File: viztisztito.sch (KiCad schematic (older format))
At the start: 18 parts

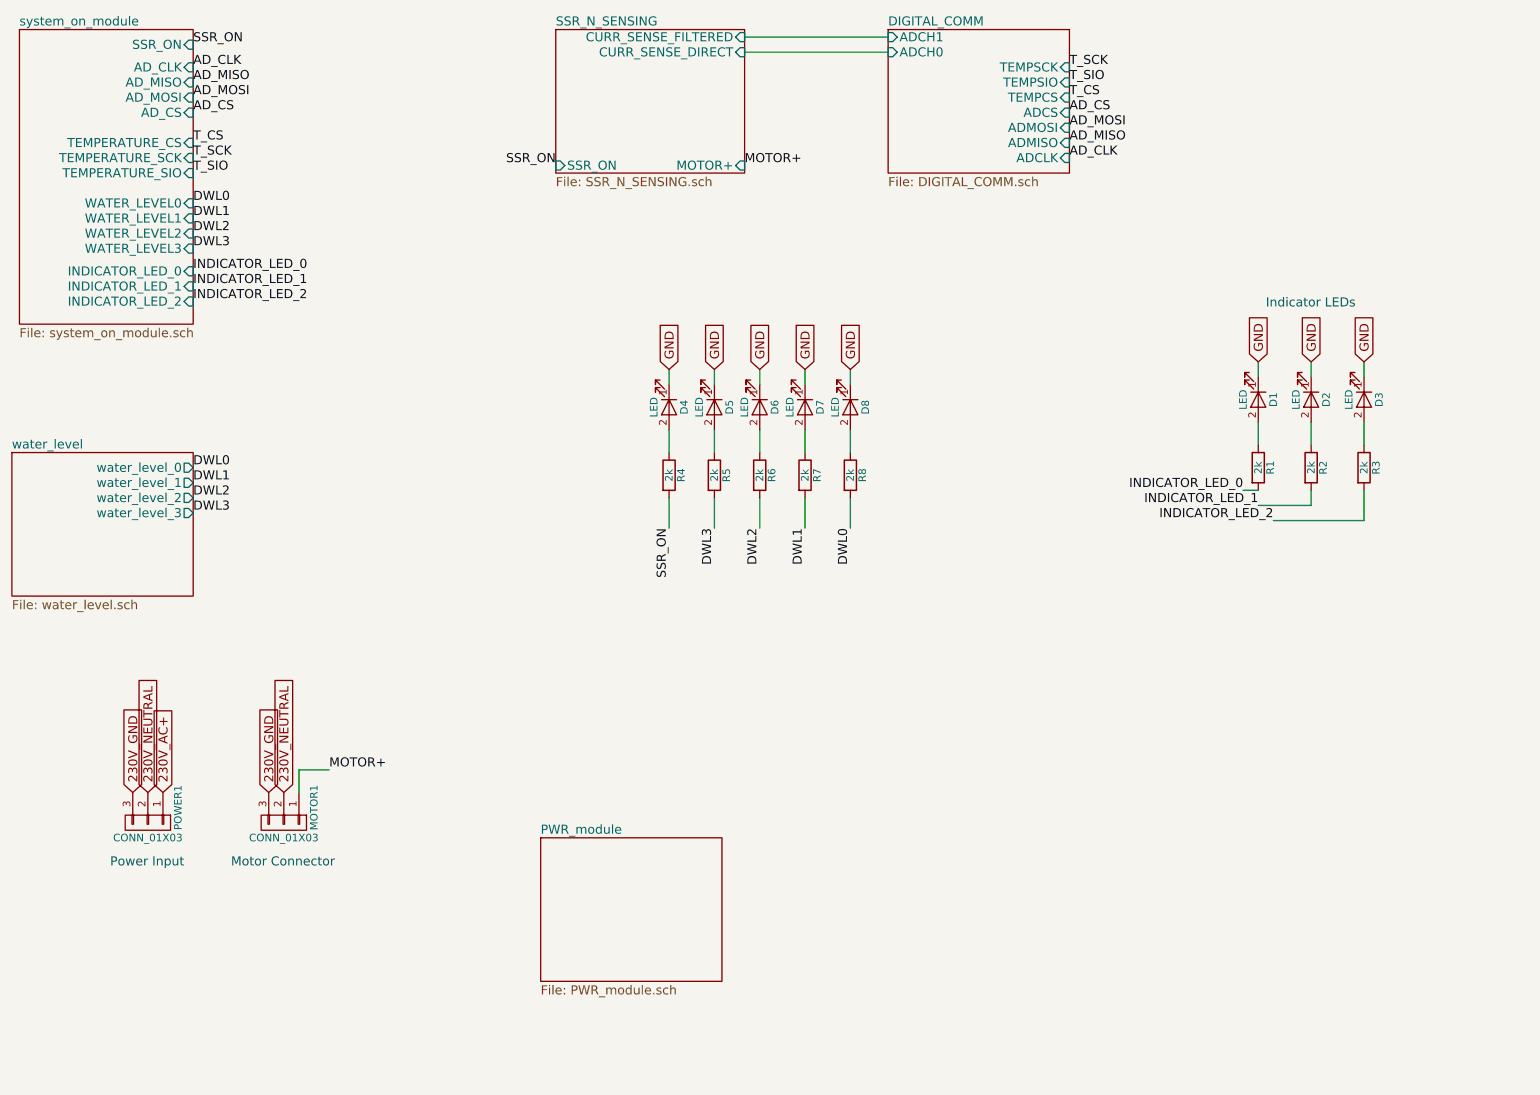
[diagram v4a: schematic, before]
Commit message: this version contains the datasheets and the footprints of the parts
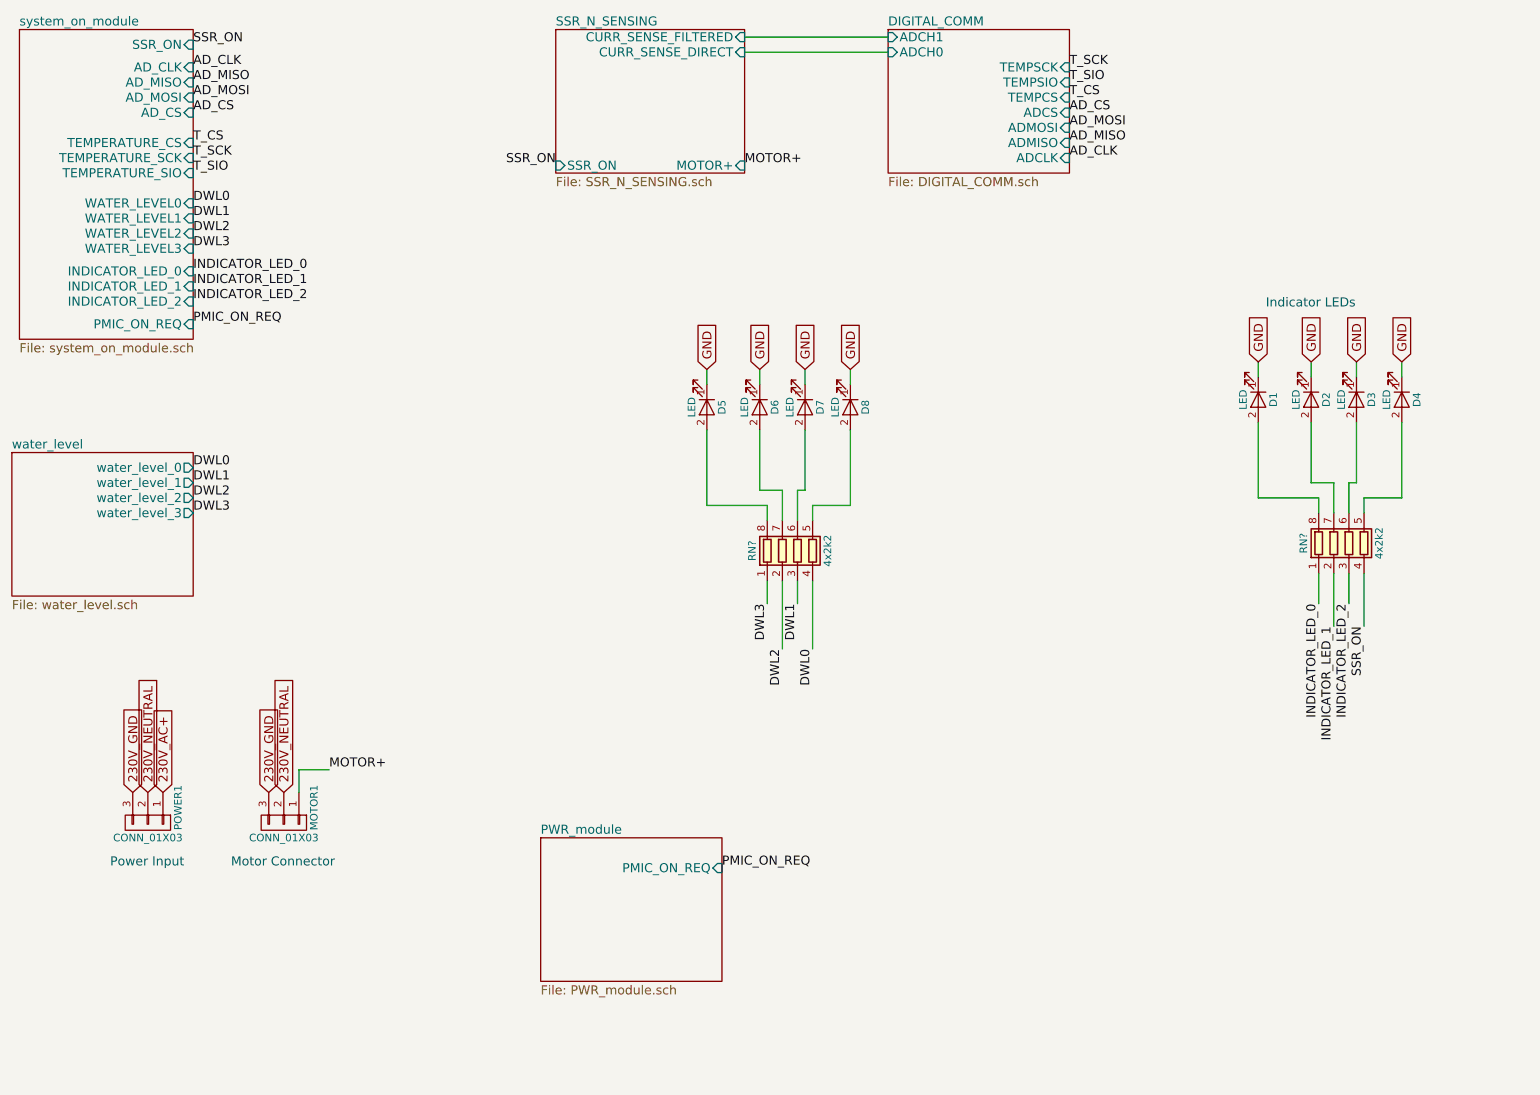
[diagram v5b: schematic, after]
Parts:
- removed R1, R2, R3, R4, R5, R6, R7, R8: 2k, Resistors_SMD:R_1206_HandSoldering, symbol R
- added RN? (x2): 4x2k2, symbol R_Pack04
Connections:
- net DWL0: now also RN?.4 (R4.1)
- net DWL1: now also RN?.3 (R3.1)
- net DWL2: now also RN?.2 (R2.1)
- net DWL3: now also RN?.1 (R1.1)
- net INDICATOR_LED_0: now also RN?.1 (R1.1)
- net INDICATOR_LED_1: now also RN?.2 (R2.1)
- net INDICATOR_LED_2: now also RN?.3 (R3.1)
- net SSR_ON: now also RN?.4 (R4.1)
- net at D2.2 (A): now also RN?.7 (R2.2)
- net at D1.2 (A): now also RN?.8 (R1.2)
- net at D3.2 (A): now also RN?.6 (R3.2)
- net at D4.2 (A): now also RN?.5 (R4.2)
- net at D5.2 (A): now also RN?.8 (R1.2)
- net at D6.2 (A): now also RN?.7 (R2.2)
- net at D7.2 (A): now also RN?.6 (R3.2)
- net at D8.2 (A): now also RN?.5 (R4.2)
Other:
- moved on the sheet: D3, D4, D5
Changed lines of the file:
@@
 F0 "PWR_module" 60
 F1 "PWR_module.sch" 60
+F2 "PMIC_ON_REQ" I R 5950 6550 60
 $EndSheet
 $Sheet
@@
 230V_GND
 $Comp
-L R R2
-U 1 1 593FD7AC
-P 9850 3900
-F 0 "R2" V 9930 3900 50  0000 C CNN
-F 1 "2k" V 9850 3900 50  0000 C CNN
-F 2 "Resistors_SMD:R_1206_HandSoldering" V 9780 3900 50  0001 C CNN
-F 3 "http://hu.farnell.com/multicomp/mcwr12x3300ftl/res-thick-film-330r-1-0-25w-1206/dp/2447504" H 9850 3900 50  0001 C CNN
-	1    9850 3900
-	1    0    0    -1
-$EndComp
-$Comp
 L LED D2
 U 1 1 593FD84F
@@
 	9850 3200 9850 3300
 Wire Wire Line
-	9850 3600 9850 3750
-$Comp
-L R R1
-U 1 1 593FEF66
-P 9500 3900
-F 0 "R1" V 9580 3900 50  0000 C CNN
-F 1 "2k" V 9500 3900 50  0000 C CNN
-F 2 "Resistors_SMD:R_1206_HandSoldering" V 9430 3900 50  0001 C CNN
-F 3 "http://hu.farnell.com/multicomp/mcwr12x3300ftl/res-thick-film-330r-1-0-25w-1206/dp/2447504" H 9500 3900 50  0001 C CNN
-	1    9500 3900
-	1    0    0    -1
-$EndComp
+	9850 3600 9850 4000
 $Comp
 L LED D1
@@
 	9500 3200 9500 3300
 Wire Wire Line
-	9500 3600 9500 3750
-$Comp
-L R R3
-U 1 1 593FF0D5
-P 10200 3900
-F 0 "R3" V 10280 3900 50  0000 C CNN
-F 1 "2k" V 10200 3900 50  0000 C CNN
-F 2 "Resistors_SMD:R_1206_HandSoldering" V 10130 3900 50  0001 C CNN
-F 3 "http://hu.farnell.com/multicomp/mcwr12x3300ftl/res-thick-film-330r-1-0-25w-1206/dp/2447504" H 10200 3900 50  0001 C CNN
-	1    10200 3900
-	1    0    0    -1
-$EndComp
+	9500 3600 9500 4100
 $Comp
 L LED D3
 U 1 1 593FF0DB
-P 10200 3450
-F 0 "D3" H 10200 3550 50  0000 C CNN
-F 1 "LED" H 10200 3350 50  0000 C CNN
-F 2 "LEDs:LED_1206" H 10200 3450 50  0001 C CNN
-F 3 "http://hu.farnell.com/lumex/sml-lx15syc-tr/led-yellow-3mm-60mcd-590nm/dp/2062220" H 10200 3450 50  0001 C CNN
-	1    10200 3450
-	0    1    1    0
-$EndComp
-Text GLabel 10200 3200 1    60   Input ~ 0
-GND
-Wire Wire Line
-	10200 3200 10200 3300
-Wire Wire Line
-	10200 3600 10200 3750
-Wire Wire Line
-	9400 4050 9500 4050
-Wire Wire Line
-	9500 4150 9850 4150
-Wire Wire Line
-	9850 4150 9850 4050
-Wire Wire Line
-	9600 4250 10200 4250
-Wire Wire Line
-	10200 4250 10200 4050
+P 10150 3450
+F 0 "D3" H 10150 3550 50  0000 C CNN
+F 1 "LED" H 10150 3350 50  0000 C CNN
+F 2 "LEDs:LED_1206" H 10150 3450 50  0001 C CNN
+F 3 "http://hu.farnell.com/lumex/sml-lx15syc-tr/led-yellow-3mm-60mcd-590nm/dp/2062220" H 10150 3450 50  0001 C CNN
+	1    10150 3450
+	0    1    1    0
+$EndComp
+Text GLabel 10150 3200 1    60   Input ~ 0
+GND
+Wire Wire Line
+	10150 3200 10150 3300
+Wire Wire Line
+	10150 3600 10150 4000
 Text Notes 9550 2850 0    60   ~ 0
 Indicator LEDs
 $Comp
-L R R4
-U 1 1 59406395
-P 5600 3950
-F 0 "R4" V 5680 3950 50  0000 C CNN
-F 1 "2k" V 5600 3950 50  0000 C CNN
-F 2 "Resistors_SMD:R_1206_HandSoldering" V 5530 3950 50  0001 C CNN
-F 3 "http://hu.farnell.com/multicomp/mcwr12x1001ftl/res-thick-film-1k-1-0-25w-1206/dp/2447473" H 5600 3950 50  0001 C CNN
-	1    5600 3950
-	1    0    0    -1
-$EndComp
-$Comp
 L LED D4
 U 1 1 5940639C
-P 5600 3500
-F 0 "D4" H 5600 3600 50  0000 C CNN
-F 1 "LED" H 5600 3400 50  0000 C CNN
-F 2 "LEDs:LED_1206" H 5600 3500 50  0001 C CNN
-F 3 "http://hu.farnell.com/lumex/sml-lx15syc-tr/led-yellow-3mm-60mcd-590nm/dp/2062220" H 5600 3500 50  0001 C CNN
-	1    5600 3500
-	0    1    1    0
-$EndComp
-Text GLabel 5600 3250 1    60   Input ~ 0
-GND
-Wire Wire Line
-	5600 3250 5600 3350
-Wire Wire Line
-	5600 3650 5600 3800
-Wire Wire Line
-	5600 4300 5600 4100
-Text Label 5600 4300 3    60   ~ 0
+P 10450 3450
+F 0 "D4" H 10450 3550 50  0000 C CNN
+F 1 "LED" H 10450 3350 50  0000 C CNN
+F 2 "LEDs:LED_1206" H 10450 3450 50  0001 C CNN
+F 3 "http://hu.farnell.com/lumex/sml-lx15syc-tr/led-yellow-3mm-60mcd-590nm/dp/2062220" H 10450 3450 50  0001 C CNN
+	1    10450 3450
+	0    1    1    0
+$EndComp
+Text GLabel 10450 3200 1    60   Input ~ 0
+GND
+Wire Wire Line
+	10450 3200 10450 3300
+Wire Wire Line
+	10450 3600 10450 4100
+Text Label 10200 4950 3    60   ~ 0
 SSR_ON
-$Comp
-L R R5
-U 1 1 59406BBF
-P 5900 3950
-F 0 "R5" V 5980 3950 50  0000 C CNN
-F 1 "2k" V 5900 3950 50  0000 C CNN
-F 2 "Resistors_SMD:R_1206_HandSoldering" V 5830 3950 50  0001 C CNN
-F 3 "http://hu.farnell.com/multicomp/mcwr12x1001ftl/res-thick-film-1k-1-0-25w-1206/dp/2447473" H 5900 3950 50  0001 C CNN
-	1    5900 3950
-	1    0    0    -1
-$EndComp
 $Comp
 L LED D5
 U 1 1 59406BC6
-P 5900 3500
-F 0 "D5" H 5900 3600 50  0000 C CNN
-F 1 "LED" H 5900 3400 50  0000 C CNN
-F 2 "LEDs:LED_1206" H 5900 3500 50  0001 C CNN
-F 3 "http://hu.farnell.com/lumex/sml-lx15syc-tr/led-yellow-3mm-60mcd-590nm/dp/2062220" H 5900 3500 50  0001 C CNN
-	1    5900 3500
-	0    1    1    0
-$EndComp
-Text GLabel 5900 3250 1    60   Input ~ 0
-GND
-Wire Wire Line
-	5900 3250 5900 3350
-Wire Wire Line
-	5900 3650 5900 3800
-Wire Wire Line
-	5900 4300 5900 4100
-$Comp
-L R R6
-U 1 1 59406CAD
-P 6200 3950
-F 0 "R6" V 6280 3950 50  0000 C CNN
-F 1 "2k" V 6200 3950 50  0000 C CNN
-F 2 "Resistors_SMD:R_1206_HandSoldering" V 6130 3950 50  0001 C CNN
-F 3 "http://hu.farnell.com/multicomp/mcwr12x1001ftl/res-thick-film-1k-1-0-25w-1206/dp/2447473" H 6200 3950 50  0001 C CNN
-	1    6200 3950
-	1    0    0    -1
-$EndComp
+P 5850 3500
+F 0 "D5" H 5850 3600 50  0000 C CNN
+F 1 "LED" H 5850 3400 50  0000 C CNN
+F 2 "LEDs:LED_1206" H 5850 3500 50  0001 C CNN
+F 3 "http://hu.farnell.com/lumex/sml-lx15syc-tr/led-yellow-3mm-60mcd-590nm/dp/2062220" H 5850 3500 50  0001 C CNN
+	1    5850 3500
+	0    1    1    0
+$EndComp
+Text GLabel 5850 3250 1    60   Input ~ 0
+GND
+Wire Wire Line
+	5850 3250 5850 3350
 $Comp
 L LED D6
@@
 Wire Wire Line
 	6200 3250 6200 3350
-Wire Wire Line
-	6200 3650 6200 3800
-Wire Wire Line
-	6200 4300 6200 4100
-$Comp
-L R R7
-U 1 1 59406D8D
-P 6500 3950
-F 0 "R7" V 6580 3950 50  0000 C CNN
-F 1 "2k" V 6500 3950 50  0000 C CNN
-F 2 "Resistors_SMD:R_1206_HandSoldering" V 6430 3950 50  0001 C CNN
-F 3 "http://hu.farnell.com/multicomp/mcwr12x1001ftl/res-thick-film-1k-1-0-25w-1206/dp/2447473" H 6500 3950 50  0001 C CNN
-	1    6500 3950
-	1    0    0    -1
-$EndComp
 $Comp
 L LED D7
@@
 Wire Wire Line
 	6500 3250 6500 3350
-Wire Wire Line
-	6500 3650 6500 3800
-Wire Wire Line
-	6500 4300 6500 4100
-$Comp
-L R R8
-U 1 1 59406E7B
-P 6800 3950
-F 0 "R8" V 6880 3950 50  0000 C CNN
-F 1 "2k" V 6800 3950 50  0000 C CNN
-F 2 "Resistors_SMD:R_1206_HandSoldering" V 6730 3950 50  0001 C CNN
-F 3 "http://hu.farnell.com/multicomp/mcwr12x1001ftl/res-thick-film-1k-1-0-25w-1206/dp/2447473" H 6800 3950 50  0001 C CNN
-	1    6800 3950
-	1    0    0    -1
-$EndComp
 $Comp
 L LED D8
@@
 Wire Wire Line
 	6800 3250 6800 3350
-Wire Wire Line
-	6800 3650 6800 3800
-Wire Wire Line
-	6800 4300 6800 4100
-Text Label 5900 4300 3    60   ~ 0
+Text Label 6250 4800 3    60   ~ 0
 DWL3
-Text Label 6200 4300 3    60   ~ 0
+Text Label 6350 5100 3    60   ~ 0
 DWL2
-Text Label 6500 4300 3    60   ~ 0
+Text Label 6450 4800 3    60   ~ 0
 DWL1
-Text Label 6800 4300 3    60   ~ 0
+Text Label 6550 5100 3    60   ~ 0
 DWL0
 $Sheet
-S 1300 1000 1150 1950
+S 1300 1000 1150 2050
 U 599A5341
 F0 "system_on_module" 60
@@
 F15 "INDICATOR_LED_1" I R 2450 2700 60
 F16 "INDICATOR_LED_2" I R 2450 2800 60
+F17 "PMIC_ON_REQ" I R 2450 2950 60
 $EndSheet
 Text Label 6100 1900 0    60   ~ 0
@@
 Text Label 2450 2800 0    60   ~ 0
 INDICATOR_LED_2
-Text Label 9400 4050 2    60   ~ 0
+Text Label 9900 4800 3    60   ~ 0
 INDICATOR_LED_0
-Text Label 9500 4150 2    60   ~ 0
+Text Label 10000 4950 3    60   ~ 0
 INDICATOR_LED_1
-Text Label 9600 4250 2    60   ~ 0
+Text Label 10100 4800 3    60   ~ 0
 INDICATOR_LED_2
+Text Label 2450 2950 0    60   ~ 0
+PMIC_ON_REQ
+Text Label 5950 6550 0    60   ~ 0
+PMIC_ON_REQ
+$Comp
+L R_Pack04 RN?
+U 1 1 59A7A20E
+P 6450 4450
+F 0 "RN?" V 6150 4450 50  0000 C CNN
+F 1 "4x2k2" V 6650 4450 50  0000 C CNN
+F 2 "" V 6725 4450 50  0001 C CNN
+F 3 "http://hu.farnell.com/yageo-phycomp/yc164-jr-072k2l/resistor-array-arv241-1206-2k2/dp/9234535" H 6450 4450 50  0001 C CNN
+	1    6450 4450
+	1    0    0    -1
+$EndComp
+$Comp
+L R_Pack04 RN?
+U 1 1 59A7A83E
+P 10100 4400
+F 0 "RN?" V 9800 4400 50  0000 C CNN
+F 1 "4x2k2" V 10300 4400 50  0000 C CNN
+F 2 "" V 10375 4400 50  0001 C CNN
+F 3 "http://hu.farnell.com/yageo-phycomp/yc164-jr-072k2l/resistor-array-arv241-1206-2k2/dp/9234535" H 10100 4400 50  0001 C CNN
+	1    10100 4400
+	1    0    0    -1
+$EndComp
+Wire Wire Line
+	10200 4950 10200 4600
+Wire Wire Line
+	10100 4800 10100 4600
+Wire Wire Line
+	10000 4950 10000 4600
+Wire Wire Line
+	9900 4800 9900 4600
+Wire Wire Line
+	10150 4000 10100 4000
+Wire Wire Line
+	10100 4000 10100 4200
+Wire Wire Line
+	9850 4000 10000 4000
+Wire Wire Line
+	10000 4000 10000 4200
+Wire Wire Line
+	9500 4100 9900 4100
+Wire Wire Line
+	9900 4100 9900 4200
+Wire Wire Line
+	10450 4100 10200 4100
+Wire Wire Line
+	10200 4100 10200 4200
+Wire Wire Line
+	6550 5100 6550 4650
+Wire Wire Line
+	6450 4800 6450 4650
+Wire Wire Line
+	6350 5100 6350 4650
+Wire Wire Line
+	6250 4800 6250 4650
+Wire Wire Line
+	6200 3650 6200 4050
+Wire Wire Line
+	5850 3650 5850 4150
+Wire Wire Line
+	6500 3650 6500 4050
+Wire Wire Line
+	6800 3650 6800 4150
+Wire Wire Line
+	6500 4050 6450 4050
+Wire Wire Line
+	6450 4050 6450 4250
+Wire Wire Line
+	6200 4050 6350 4050
+Wire Wire Line
+	6350 4050 6350 4250
+Wire Wire Line
+	5850 4150 6250 4150
+Wire Wire Line
+	6250 4150 6250 4250
+Wire Wire Line
+	6800 4150 6550 4150
+Wire Wire Line
+	6550 4150 6550 4250
 $EndSCHEMATC

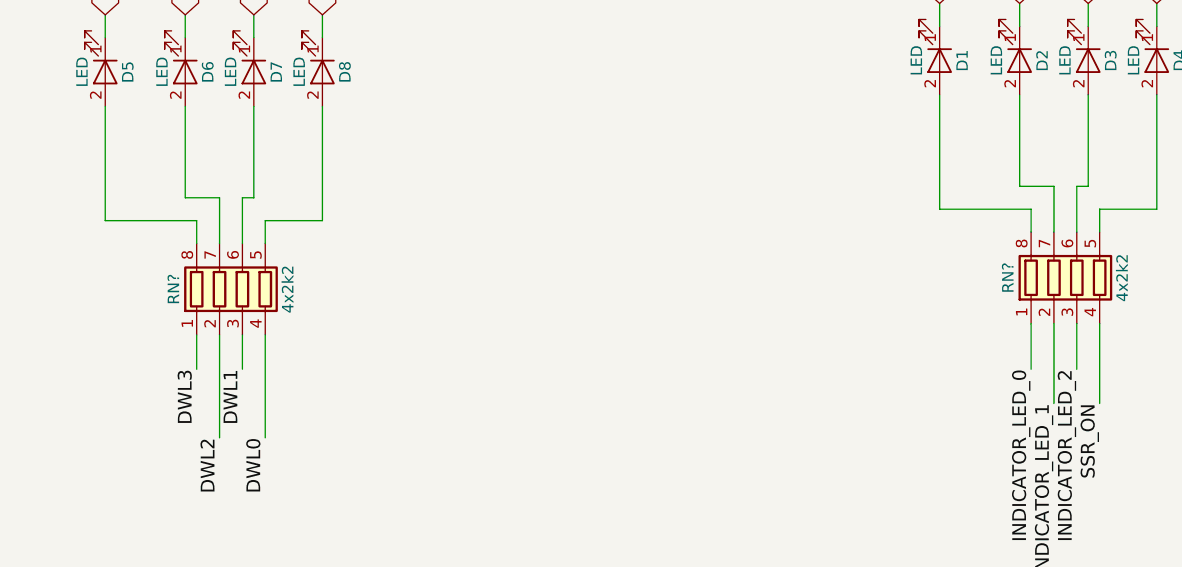
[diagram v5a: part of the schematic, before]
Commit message: some issues fixed by the bugfixer; formal verification needed
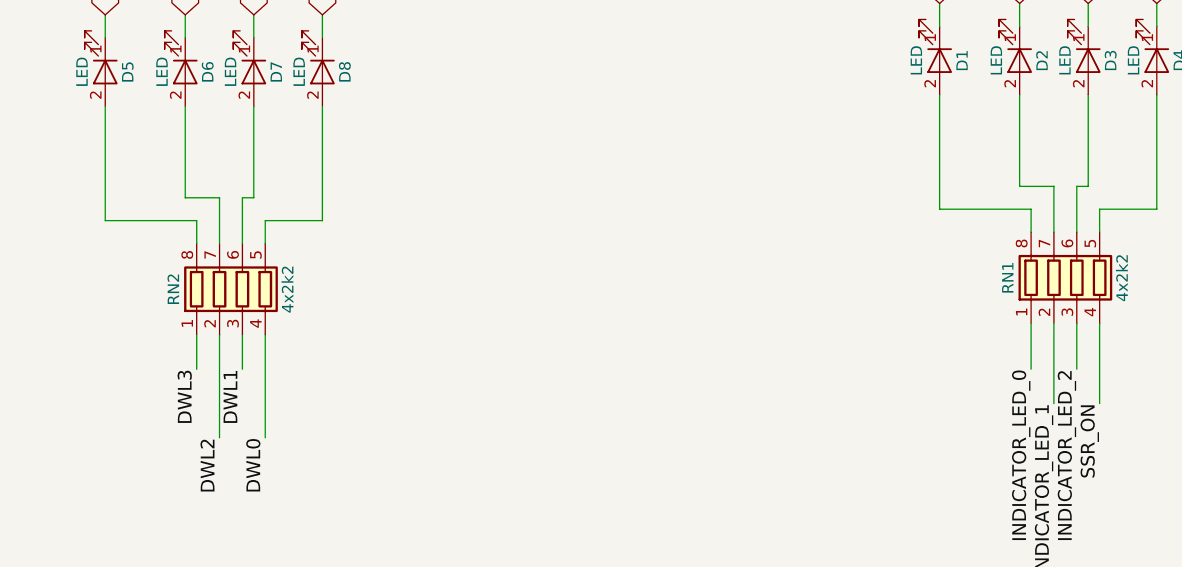
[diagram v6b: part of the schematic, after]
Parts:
- gave numbers to parts that had none: 2
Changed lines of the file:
@@
 PMIC_ON_REQ
 $Comp
-L R_Pack04 RN?
+L R_Pack04 RN2
 U 1 1 59A7A20E
 P 6450 4450
-F 0 "RN?" V 6150 4450 50  0000 C CNN
+F 0 "RN2" V 6150 4450 50  0000 C CNN
 F 1 "4x2k2" V 6650 4450 50  0000 C CNN
 F 2 "" V 6725 4450 50  0001 C CNN
@@
 $EndComp
 $Comp
-L R_Pack04 RN?
+L R_Pack04 RN1
 U 1 1 59A7A83E
 P 10100 4400
-F 0 "RN?" V 9800 4400 50  0000 C CNN
+F 0 "RN1" V 9800 4400 50  0000 C CNN
 F 1 "4x2k2" V 10300 4400 50  0000 C CNN
 F 2 "" V 10375 4400 50  0001 C CNN

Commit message: I have verified the schematic a second time (except the so-dimm), and I have selected all of the components with links and footprint. I need to verify the schematic a third time and root
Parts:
- RN1, RN2: footprint (none) -> kilibs:YC164-Yageo-Handsoldering
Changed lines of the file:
@@
 F 0 "RN2" V 6150 4450 50  0000 C CNN
 F 1 "4x2k2" V 6650 4450 50  0000 C CNN
-F 2 "" V 6725 4450 50  0001 C CNN
+F 2 "kilibs:YC164-Yageo-Handsoldering" V 6725 4450 50  0001 C CNN
 F 3 "http://hu.farnell.com/yageo-phycomp/yc164-jr-072k2l/resistor-array-arv241-1206-2k2/dp/9234535" H 6450 4450 50  0001 C CNN
 	1    6450 4450
@@
 F 0 "RN1" V 9800 4400 50  0000 C CNN
 F 1 "4x2k2" V 10300 4400 50  0000 C CNN
-F 2 "" V 10375 4400 50  0001 C CNN
+F 2 "kilibs:YC164-Yageo-Handsoldering" V 10375 4400 50  0001 C CNN
 F 3 "http://hu.farnell.com/yageo-phycomp/yc164-jr-072k2l/resistor-array-arv241-1206-2k2/dp/9234535" H 10100 4400 50  0001 C CNN
 	1    10100 4400
